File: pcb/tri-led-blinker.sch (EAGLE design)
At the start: 13 parts, among them J1 MICRO-USB-SMD(ZX62-B-5PA), K1 TS-1109

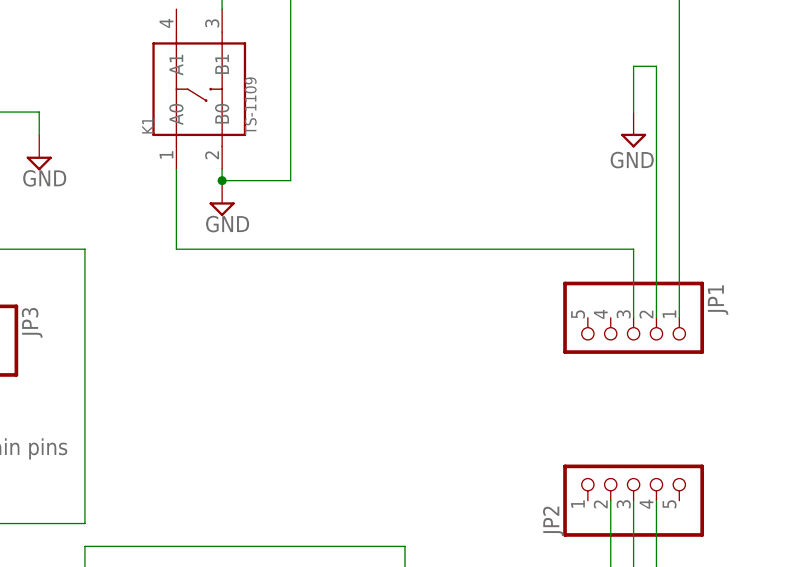
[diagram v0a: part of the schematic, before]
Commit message: change button input pin to PB3
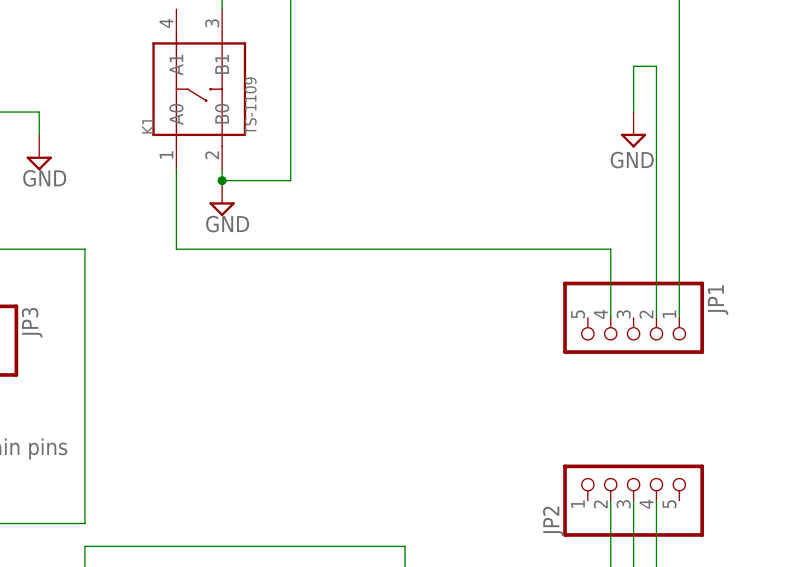
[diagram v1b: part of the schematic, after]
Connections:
- net N$5: now also JP1.4; no longer JP1.3
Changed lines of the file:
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@@
 <segment>
 <pinref part="K1" gate="G$1" pin="A0"/>
-<pinref part="JP1" gate="A" pin="3"/>
 <wire x1="101.6" y1="73.66" x2="101.6" y2="82.55" width="0.1524" layer="91"/>
-<wire x1="152.4" y1="66.04" x2="152.4" y2="73.66" width="0.1524" layer="91"/>
-<wire x1="152.4" y1="73.66" x2="101.6" y2="73.66" width="0.1524" layer="91"/>
+<pinref part="JP1" gate="A" pin="4"/>
+<wire x1="101.6" y1="73.66" x2="149.86" y2="73.66" width="0.1524" layer="91"/>
+<wire x1="149.86" y1="73.66" x2="149.86" y2="66.04" width="0.1524" layer="91"/>
 </segment>
 </net>
